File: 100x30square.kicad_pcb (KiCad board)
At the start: 2 copper layers, 100 x 30 mm, 56 parts

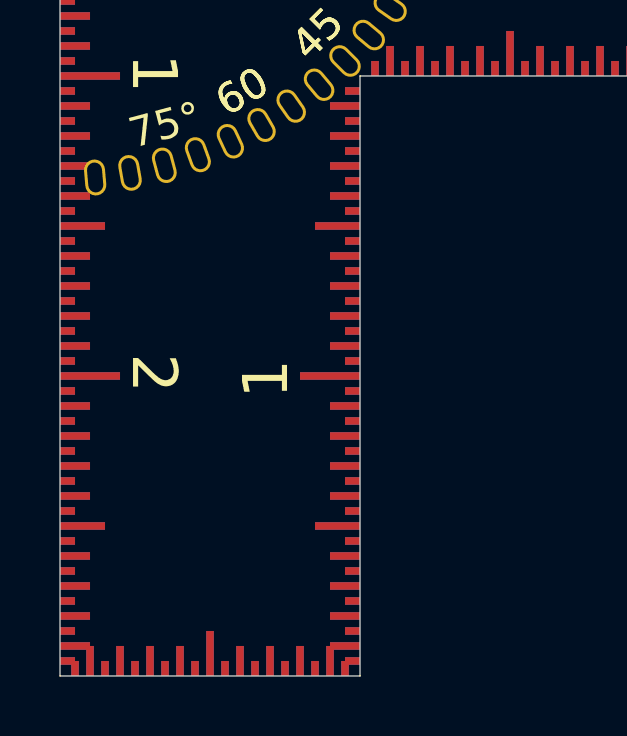
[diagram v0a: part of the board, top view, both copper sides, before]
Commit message: Add a metric and imperial trace gauge
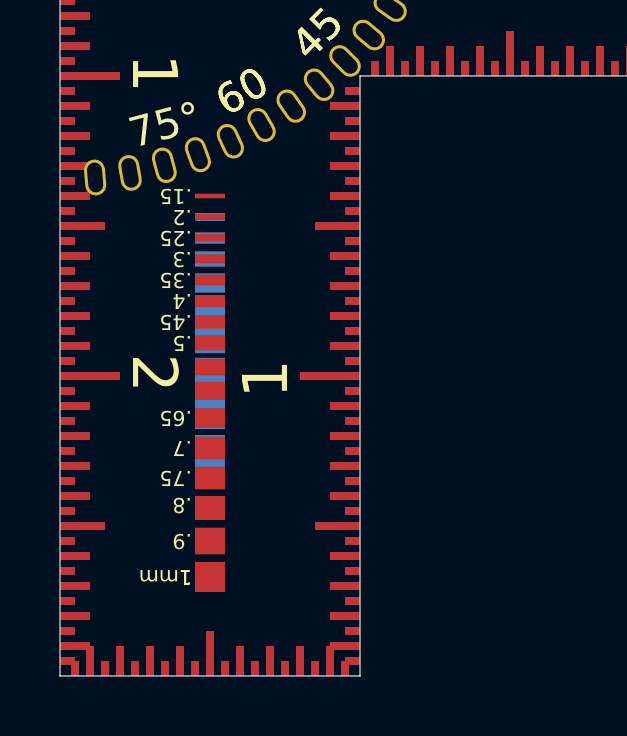
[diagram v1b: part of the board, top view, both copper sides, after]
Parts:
- added REF**: trace_gauge_0.15_1mm, Library:trace_gauge_0.15_1mm, F.Cu at (55.0, 64.0)
- added REF**: trace_gauge_15_50mil, Library:trace_gauge_15_50mil, B.Cu at (55.0, 64.0)
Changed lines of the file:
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@@
       (clearance 0.01))
+  )
+  (footprint "Library:trace_gauge_0.15_1mm" (layer "F.Cu")
+    (at 55 64 180)
+    (attr smd)
+    (fp_text reference "REF**" (at 0 -0.5 180 unlocked) (layer "F.SilkS") hide
+        (effects (font (size 1 1) (thickness 0.1)))
+    )
+    (fp_text value "trace_gauge_0.15_1mm" (at 0 1 180 unlocked) (layer "F.Fab") hide
+        (effects (font (size 1 1) (thickness 0.15)))
+    )
+    (fp_text user ".75" (at 0.6 -9.4 180 unlocked) (layer "F.SilkS")
+        (effects (font (size 0.5 0.5) (thickness 0.1)) (justify left))
+    )
+    (fp_text user "1mm" (at 0.6 -12.7 180 unlocked) (layer "F.SilkS")
+        (effects (font (size 0.5 0.5) (thickness 0.1)) (justify left))
+    )
+    (fp_text user ".4" (at 0.6 -3.5 180 unlocked) (layer "F.SilkS")
+        (effects (font (size 0.5 0.5) (thickness 0.1)) (justify left))
+    )
+    (fp_text user ".65" (at 0.6 -7.4 180 unlocked) (layer "F.SilkS")
+        (effects (font (size 0.5 0.5) (thickness 0.1)) (justify left))
+    )
+    (fp_text user ".5" (at 0.6 -4.9 180 unlocked) (layer "F.SilkS")
+        (effects (font (size 0.5 0.5) (thickness 0.1)) (justify left))
+    )
+    (fp_text user ".7" (at 0.6 -8.4 180 unlocked) (layer "F.SilkS")
+        (effects (font (size 0.5 0.5) (thickness 0.1)) (justify left))
+    )
+    (fp_text user ".3" (at 0.6 -2.1 180 unlocked) (layer "F.SilkS")
+        (effects (font (size 0.5 0.5) (thickness 0.1)) (justify left))
+    )
+    (fp_text user ".8" (at 0.6 -10.3 180 unlocked) (layer "F.SilkS")
+        (effects (font (size 0.5 0.5) (thickness 0.1)) (justify left))
+    )
+    (fp_text user "1" (at 0.6 -12.7 180 unlocked) (layer "F.SilkS")
+        (effects (font (size 0.5 0.5) (thickness 0.1)) (justify left))
+    )
+    (fp_text user ".45" (at 0.6 -4.2 180 unlocked) (layer "F.SilkS")
+        (effects (font (size 0.5 0.5) (thickness 0.1)) (justify left))
+    )
+    (fp_text user ".2" (at 0.6 -0.7 180 unlocked) (layer "F.SilkS")
+        (effects (font (size 0.5 0.5) (thickness 0.1)) (justify left))
+    )
+    (fp_text user ".35" (at 0.6 -2.8 180 unlocked) (layer "F.SilkS")
+        (effects (font (size 0.5 0.5) (thickness 0.1)) (justify left))
+    )
+    (fp_text user ".15" (at 0.6 0 180 unlocked) (layer "F.SilkS")
+        (effects (font (size 0.5 0.5) (thickness 0.1)) (justify left))
+    )
+    (fp_text user ".25" (at 0.6 -1.4 180 unlocked) (layer "F.SilkS")
+        (effects (font (size 0.5 0.5) (thickness 0.1)) (justify left))
+    )
+    (fp_text user ".9" (at 0.6 -11.5 180 unlocked) (layer "F.SilkS")
+        (effects (font (size 0.5 0.5) (thickness 0.1)) (justify left))
+    )
+    (fp_text user "${REFERENCE}" (at 0 2.5 180 unlocked) (layer "F.Fab") hide
+        (effects (font (size 1 1) (thickness 0.15)))
+    )
+    (pad "" smd rect (at 0 -12.7 180) (size 1 1) (layers "F.Cu" "F.Paste" "F.Mask")
+      (thermal_bridge_angle 45))
+    (pad "" smd rect (at 0 -11.5 180) (size 1 0.9) (layers "F.Cu" "F.Paste" "F.Mask")
+      (thermal_bridge_angle 45))
+    (pad "" smd rect (at 0 -10.4 180) (size 1 0.8) (layers "F.Cu" "F.Paste" "F.Mask")
+      (thermal_bridge_angle 45))
+    (pad "" smd rect (at 0 -9.4 180) (size 1 0.75) (layers "F.Cu" "F.Paste" "F.Mask")
+      (thermal_bridge_angle 45))
+    (pad "" smd rect (at 0 -8.4 180) (size 1 0.75) (layers "F.Cu" "F.Paste" "F.Mask")
+      (thermal_bridge_angle 45))
+    (pad "" smd rect (at 0 -7.4 180) (size 1 0.65) (layers "F.Cu" "F.Paste" "F.Mask")
+      (thermal_bridge_angle 45))
+    (pad "" smd rect (at 0 -6.5 180) (size 1 0.6) (layers "F.Cu" "F.Paste" "F.Mask")
+      (thermal_bridge_angle 45))
+    (pad "" smd rect (at 0 -5.7 180) (size 1 0.55) (layers "F.Cu" "F.Paste" "F.Mask")
+      (thermal_bridge_angle 45))
+    (pad "" smd rect (at 0 -4.9 180) (size 1 0.5) (layers "F.Cu" "F.Paste" "F.Mask")
+      (thermal_bridge_angle 45))
+    (pad "" smd rect (at 0 -4.2 180) (size 1 0.45) (layers "F.Cu" "F.Paste" "F.Mask")
+      (thermal_bridge_angle 45))
+    (pad "" smd rect (at 0 -3.5 180) (size 1 0.4) (layers "F.Cu" "F.Paste" "F.Mask")
+      (thermal_bridge_angle 45))
+    (pad "" smd rect (at 0 -2.8 180) (size 1 0.35) (layers "F.Cu" "F.Paste" "F.Mask")
+      (thermal_bridge_angle 45))
+    (pad "" smd rect (at 0 -2.1 180) (size 1 0.3) (layers "F.Cu" "F.Paste" "F.Mask")
+      (thermal_bridge_angle 45))
+    (pad "" smd rect (at 0 -1.4 180) (size 1 0.25) (layers "F.Cu" "F.Paste" "F.Mask")
+      (thermal_bridge_angle 45))
+    (pad "" smd rect (at 0 -0.7 180) (size 1 0.2) (layers "F.Cu" "F.Paste" "F.Mask")
+      (thermal_bridge_angle 45))
+    (pad "" smd rect (at 0 0 180) (size 1 0.15) (layers "F.Cu" "F.Paste" "F.Mask")
+      (thermal_bridge_angle 45))
   )
   (footprint "Library:1cm" (layer "F.Cu")
@@
       (clearance 0.01))
   )
+  (footprint "Library:trace_gauge_15_50mil" (layer "B.Cu")
+    (at 55 64)
+    (attr smd)
+    (fp_text reference "REF**" (at 0 0.5 180 unlocked) (layer "B.SilkS") hide
+        (effects (font (size 1 1) (thickness 0.1)) (justify mirror))
+    )
+    (fp_text value "trace_gauge_15_50mil" (at 0 -1 180 unlocked) (layer "B.Fab") hide
+        (effects (font (size 1 1) (thickness 0.15)) (justify mirror))
+    )
+    (fp_text user "45" (at -0.6 7.2 180 unlocked) (layer "B.SilkS")
+        (effects (font (size 0.5 0.5) (thickness 0.1)) (justify right mirror))
+    )
+    (fp_text user "15" (at -0.6 1.4 180 unlocked) (layer "B.SilkS")
+        (effects (font (size 0.5 0.5) (thickness 0.1)) (justify right mirror))
+    )
+    (fp_text user "30" (at -0.6 3.8 180 unlocked) (layer "B.SilkS")
+        (effects (font (size 0.5 0.5) (thickness 0.1)) (justify right mirror))
+    )
+    (fp_text user "25" (at -0.6 2.9 180 unlocked) (layer "B.SilkS")
+        (effects (font (size 0.5 0.5) (thickness 0.1)) (justify right mirror))
+    )
+    (fp_text user "20" (at -0.6 2.1 180 unlocked) (layer "B.SilkS")
+        (effects (font (size 0.5 0.5) (thickness 0.1)) (justify right mirror))
+    )
+    (fp_text user "5" (at -0.6 0 180 unlocked) (layer "B.SilkS")
+        (effects (font (size 0.5 0.5) (thickness 0.1)) (justify right mirror))
+    )
+    (fp_text user "35" (at -0.6 4.8 180 unlocked) (layer "B.SilkS")
+        (effects (font (size 0.5 0.5) (thickness 0.1)) (justify right mirror))
+    )
+    (fp_text user "50" (at -0.6 8.6 180 unlocked) (layer "B.SilkS")
+        (effects (font (size 0.5 0.5) (thickness 0.1)) (justify right mirror))
+    )
+    (fp_text user "mil" (at 0.6 8.6 180 unlocked) (layer "B.SilkS")
+        (effects (font (size 0.5 0.5) (thickness 0.1)) (justify left mirror))
+    )
+    (fp_text user "10" (at -0.6 0.7 180 unlocked) (layer "B.SilkS")
+        (effects (font (size 0.5 0.5) (thickness 0.1)) (justify right mirror))
+    )
+    (fp_text user "${REFERENCE}" (at 0 -2.5 180 unlocked) (layer "B.Fab") hide
+        (effects (font (size 1 1) (thickness 0.15)) (justify mirror))
+    )
+    (pad "" smd rect (at 0 0) (size 1 0.127) (layers "B.Cu" "B.Paste" "B.Mask")
+      (thermal_bridge_angle 45))
+    (pad "" smd rect (at 0 0.7) (size 1 0.254) (layers "B.Cu" "B.Paste" "B.Mask")
+      (thermal_bridge_angle 45))
+    (pad "" smd rect (at 0 1.4) (size 1 0.381) (layers "B.Cu" "B.Paste" "B.Mask")
+      (thermal_bridge_angle 45))
+    (pad "" smd rect (at 0 2.1) (size 1 0.508) (layers "B.Cu" "B.Paste" "B.Mask")
+      (thermal_bridge_angle 45))
+    (pad "" smd rect (at 0 2.9) (size 1 0.635) (layers "B.Cu" "B.Paste" "B.Mask")
+      (thermal_bridge_angle 45))
+    (pad "" smd rect (at 0 3.8) (size 1 0.762) (layers "B.Cu" "B.Paste" "B.Mask")
+      (thermal_bridge_angle 45))
+    (pad "" smd rect (at 0 4.8) (size 1 0.889) (layers "B.Cu" "B.Paste" "B.Mask")
+      (thermal_bridge_angle 45))
+    (pad "" smd rect (at 0 5.9) (size 1 1.016) (layers "B.Cu" "B.Paste" "B.Mask")
+      (thermal_bridge_angle 45))
+    (pad "" smd rect (at 0 7.2) (size 1 1.143) (layers "B.Cu" "B.Paste" "B.Mask")
+      (thermal_bridge_angle 45))
+    (pad "" smd rect (at 0 8.6) (size 1 1.27) (layers "B.Cu" "B.Paste" "B.Mask")
+      (thermal_bridge_angle 45))
+  )
   (footprint "Library:1cm" (layer "B.Cu")

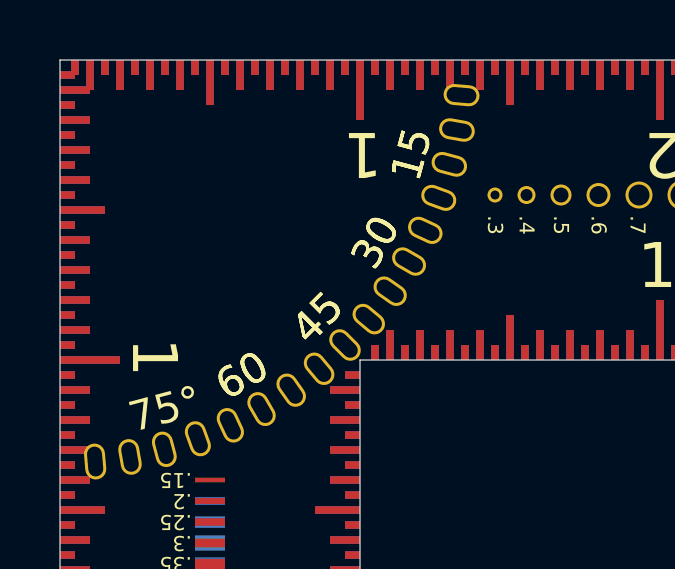
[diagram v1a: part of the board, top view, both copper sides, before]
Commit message: Add text size and thickness examples
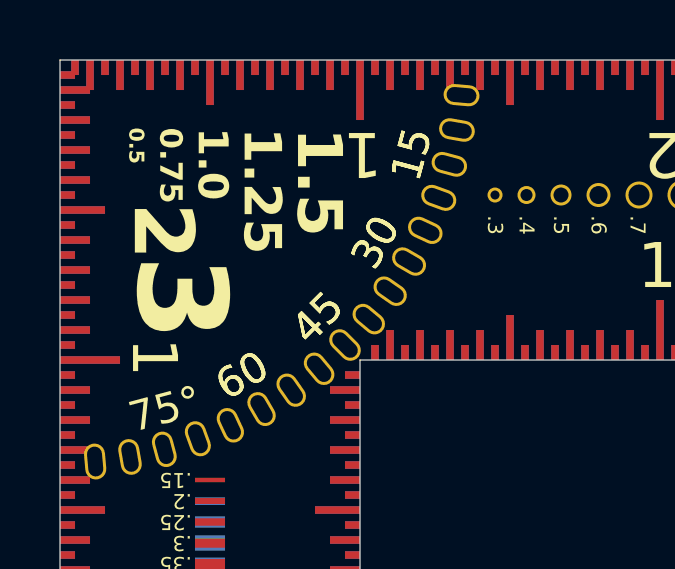
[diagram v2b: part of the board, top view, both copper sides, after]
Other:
- board text added: ".1"
- board text added: ".15"
- board text added: ".2"
- board text added: ".25"
- board text added: ".3"
- board text added: ".35"
- board text added: ".4"
- board text added: "0.5"
- board text added: "0.75"
- board text added: "1.0"
- board text added: "1.25"
- board text added: "1.5"
- board text added: "2"
- board text added: "3"
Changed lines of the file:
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@@
   (gr_line (start 50 50) (end 150 50)
     (stroke (width 0.001) (type default)) (layer "Edge.Cuts"))
+  (gr_text ".25" (at 52.25 57 180) (layer "B.SilkS")
+    (effects (font (size 1 1) (thickness 0.25) bold) (justify left bottom mirror))
+  )
+  (gr_text ".15" (at 52.25 53.75 180) (layer "B.SilkS")
+    (effects (font (size 1 1) (thickness 0.15)) (justify left bottom mirror))
+  )
+  (gr_text ".2" (at 52.25 55.25 180) (layer "B.SilkS")
+    (effects (font (size 1 1) (thickness 0.2) bold) (justify left bottom mirror))
+  )
+  (gr_text ".35" (at 54.75 54.5 180) (layer "B.SilkS")
+    (effects (font (size 1.5 1.5) (thickness 0.35) bold) (justify left bottom mirror))
+  )
+  (gr_text ".1" (at 52.25 52.25 180) (layer "B.SilkS")
+    (effects (font (size 1 1) (thickness 0.1)) (justify left bottom mirror))
+  )
+  (gr_text ".4" (at 54.75 56.5 180) (layer "B.SilkS")
+    (effects (font (size 2 2) (thickness 0.4) bold) (justify left bottom mirror))
+  )
+  (gr_text ".3" (at 54.75 52.25 180) (layer "B.SilkS")
+    (effects (font (size 1.5 1.5) (thickness 0.3) bold) (justify left bottom mirror))
+  )
+  (gr_text "3" (at 52.25 56.5 270) (layer "F.SilkS")
+    (effects (font (size 3 3) (thickness 0.2) bold) (justify left bottom))
+  )
+  (gr_text "0.75\n" (at 53.25 52.25 270) (layer "F.SilkS")
+    (effects (font (size 0.75 0.75) (thickness 0.1875) bold) (justify left bottom))
+  )
+  (gr_text "1.5" (at 57.75 52.25 270) (layer "F.SilkS")
+    (effects (font (size 1.5 1.5) (thickness 0.2) bold) (justify left bottom))
+  )
+  (gr_text "0.5	" (at 52.25 52.25 -90) (layer "F.SilkS")
+    (effects (font (size 0.5 0.5) (thickness 0.125) bold) (justify left bottom))
+  )
+  (gr_text "1.25" (at 56 52.25 270) (layer "F.SilkS")
+    (effects (font (size 1.25 1.25) (thickness 0.2) bold) (justify left bottom))
+  )
+  (gr_text "2" (at 52.25 54.75 270) (layer "F.SilkS")
+    (effects (font (size 2 2) (thickness 0.2) bold) (justify left bottom))
+  )
+  (gr_text "1.0	" (at 54.5 52.25 270) (layer "F.SilkS")
+    (effects (font (size 1 1) (thickness 0.2) bold) (justify left bottom))
+  )
 )
